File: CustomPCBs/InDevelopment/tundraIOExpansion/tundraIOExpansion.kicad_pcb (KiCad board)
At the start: 4 copper layers, 46 x 36.5 mm, 54 parts, among them J1 Conn_01x25, J2 Conn_ARM_SWD_TagConnect_TC203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, J3 Conn_ARM_SWD_TagConnect_TC203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, U1 RP2040, U2 MX25L3233FM2, U4 MX25L3233FM2, U5 RP2040, Y1 12.000MHz, Y2 12.000MHz, Y3 32.768kHz

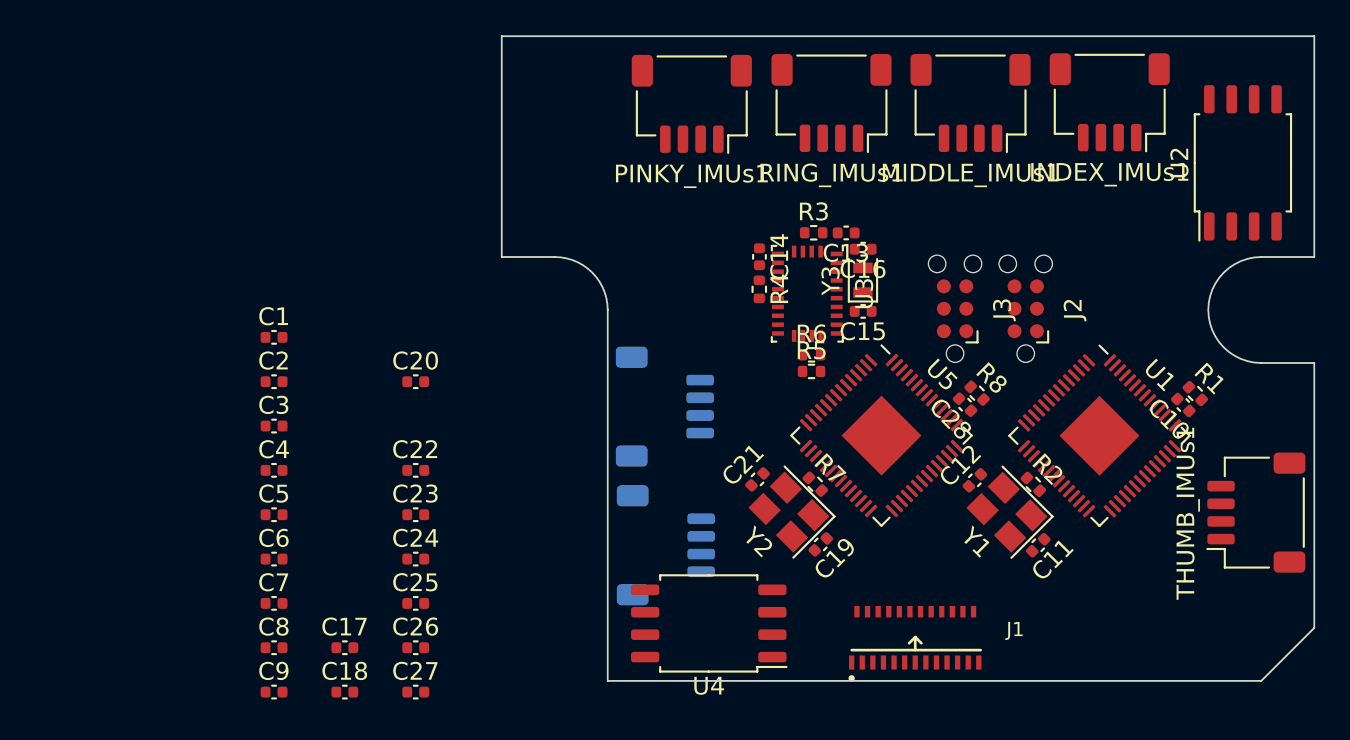
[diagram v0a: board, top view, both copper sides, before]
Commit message: Component placement complete
Will still experiment with inputs first so I know what kind of
connectors will be needed to get whatever buttons or joysticks may be
inplemented. Only after that's done will the routing of the tracks
start.
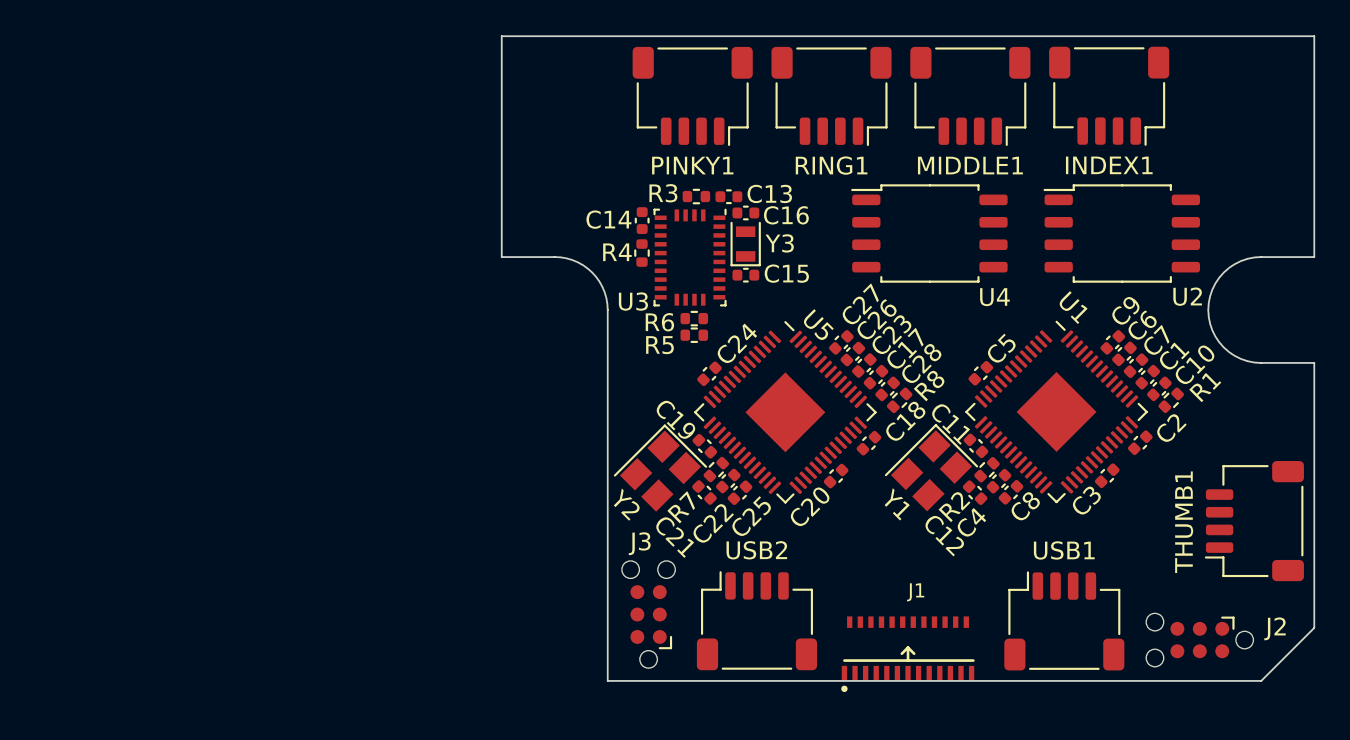
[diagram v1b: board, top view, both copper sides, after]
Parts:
- USB1, USB2: moved to F.Cu
- moved C9 51.4 mm to (150.4, 73.9), turned to 45 degrees
- moved C7 50.6 mm to (151.7, 75.2), turned to 45 degrees
- moved C6 49.5 mm to (151.0, 74.6), turned to 45 degrees
- moved C1 49.5 mm to (152.4, 75.9), turned to 45 degrees
- moved C2 49.2 mm to (151.9, 79.6), turned to -135 degrees
- moved C3 47.3 mm to (150.1, 81.5), turned to 45 degrees
- moved C8 42.6 mm to (144.6, 82.4), turned to -135 degrees
- moved C4 41.0 mm to (143.9, 81.8), turned to -135 degrees
- moved C5 40.8 mm to (142.9, 75.7), turned to -135 degrees
- moved C17 33.7 mm to (137.0, 75.9), turned to 45 degrees
- moved C18 32.8 mm to (136.6, 79.6), turned to -135 degrees
- moved C27 31.2 mm to (135.0, 73.9), turned to 45 degrees
- moved C26 29.8 mm to (135.7, 74.6), turned to 45 degrees
- moved C23 26.8 mm to (136.3, 75.2), turned to 45 degrees
- moved USB1 25.7 mm to (147.6, 89.7), turned to 0 degrees
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- renumbered INDEX_IMUs1 to INDEX1, MIDDLE_IMUs1 to MIDDLE1, PINKY_IMUs1 to PINKY1, RING_IMUs1 to RING1, THUMB_IMUs1 to THUMB1

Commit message: Adding auxiliary connectors for mixed inputs
I am still not sure what input types I will have, but I am preparing the
board to be flexible, exposing 8 GPIOs, 4 of which are analog to digital
converters.

I have also started to design the hardware interface with a second board
that can be placed below the main one, to add two rp2040 to the project
if needed.
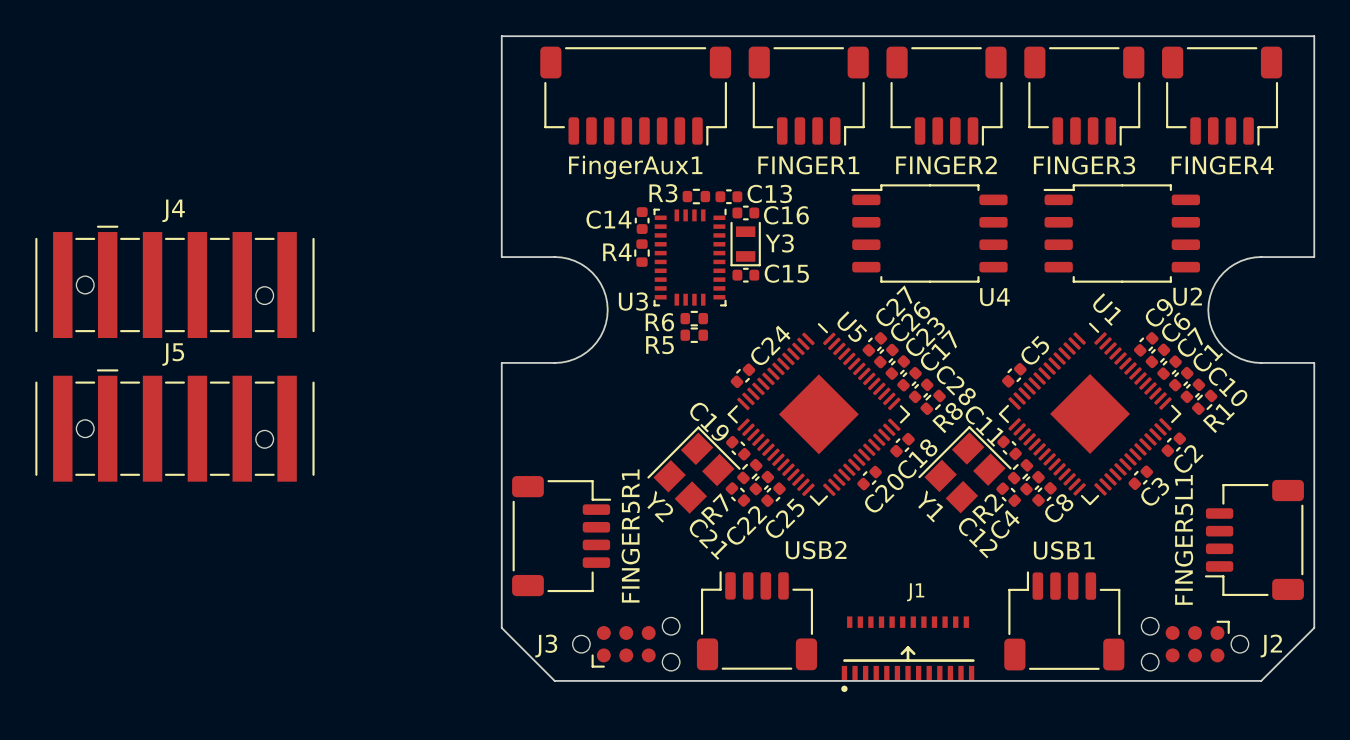
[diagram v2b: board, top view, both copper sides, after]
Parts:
- removed INDEX1, MIDDLE1, PINKY1, RING1, THUMB1: Conn_01x04, Connector_JST:JST_SH_SM04B-SRSS-TB_1x04-1MP_P1.00mm_Horizontal
- added FINGER1: Conn_01x04, Connector_JST:JST_SH_SM04B-SRSS-TB_1x04-1MP_P1.00mm_Horizontal, F.Cu at (133.2, 60.0)
- added FINGER2: Conn_01x04, Connector_JST:JST_SH_SM04B-SRSS-TB_1x04-1MP_P1.00mm_Horizontal, F.Cu at (141.0, 60.0)
- added FINGER3: Conn_01x04, Connector_JST:JST_SH_SM04B-SRSS-TB_1x04-1MP_P1.00mm_Horizontal, F.Cu at (148.8, 60.0)
- added FINGER4: Conn_01x04, Connector_JST:JST_SH_SM04B-SRSS-TB_1x04-1MP_P1.00mm_Horizontal, F.Cu at (156.6, 60.0)
- added FINGER5L1: Conn_01x04, Connector_JST:JST_SH_SM04B-SRSS-TB_1x04-1MP_P1.00mm_Horizontal, F.Cu at (158.4, 85.1)
- added FINGER5R1: Conn_01x04, Connector_JST:JST_SH_SM04B-SRSS-TB_1x04-1MP_P1.00mm_Horizontal, F.Cu at (119.1, 84.9)
- added FingerAux1: Conn_01x08, Connector_JST:JST_SH_SM08B-SRSS-TB_1x08-1MP_P1.00mm_Horizontal, F.Cu at (123.4, 60.0)
- added J4: 2211SM-04G-B1-TB, Connector_Harting:Harting_har-flexicon_14110413001xxx_1x04-MP_P2.54mm_Vertical, F.Cu at (97.3, 70.7)
- added J5: 2211SM-04G-B1-TB, Connector_Harting:Harting_har-flexicon_14110413001xxx_1x04-MP_P2.54mm_Vertical, F.Cu at (97.3, 78.8)
- moved J3 2.10 mm to (122.8, 91.0), turned to 0 degrees
- moved C10 1.90 mm to (154.9, 76.7)
- moved C12 1.90 mm to (144.5, 82.5)
- moved C18 1.90 mm to (138.5, 79.7)
- moved C23 1.90 mm to (138.2, 75.3)
- moved C6 1.90 mm to (152.9, 74.7)
- moved R7 1.90 mm to (129.8, 81.2)
- moved R8 1.90 mm to (140.2, 77.3)
- moved U5 1.90 mm to (133.7, 78.0)
- moved Y1 1.90 mm to (142.0, 81.3)
- moved C8 1.90 mm to (146.5, 82.5)
- moved C19 1.90 mm to (129.2, 79.9)
- moved C24 1.90 mm to (129.4, 75.8)
- moved Y2 1.90 mm to (126.7, 81.3)
- moved C1 1.90 mm to (154.2, 76.0)
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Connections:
- U1 pad 27: unconnected-(U1-GPIO16-Pad27) -> INTER_RP2040_UART_TX2
- U1 pad 28: unconnected-(U1-GPIO17-Pad28) -> INTER_RP2040_UART_RX2
- U1 pad 6: unconnected-(U1-GPIO4-Pad6) -> INTER_RP2040_UART_TX1
- U1 pad 7: unconnected-(U1-GPIO5-Pad7) -> INTER_RP2040_UART_RX1
- U5 pad 16: unconnected-(U5-GPIO13-Pad16) -> INTER_RP2040_UART_TX3
- U5 pad 17: unconnected-(U5-GPIO14-Pad17) -> INTER_RP2040_UART_RX3
- U5 pad 34: unconnected-(U5-GPIO22-Pad34) -> Net-(FingerAux1-Pin_1)
- U5 pad 35: unconnected-(U5-GPIO23-Pad35) -> Net-(FingerAux1-Pin_2)
- U5 pad 36: unconnected-(U5-GPIO24-Pad36) -> Net-(FingerAux1-Pin_3)
- U5 pad 37: unconnected-(U5-GPIO25-Pad37) -> Net-(FingerAux1-Pin_4)
- U5 pad 38: unconnected-(U5-GPIO26_ADC0-Pad38) -> Net-(FingerAux1-Pin_5)
- U5 pad 39: unconnected-(U5-GPIO27_ADC1-Pad39) -> Net-(FingerAux1-Pin_6)
- U5 pad 40: unconnected-(U5-GPIO28_ADC2-Pad40) -> Net-(FingerAux1-Pin_7)
- U5 pad 41: unconnected-(U5-GPIO29_ADC3-Pad41) -> Net-(FingerAux1-Pin_8)
- U5 pad 6: unconnected-(U5-GPIO4-Pad6) -> INTER_RP2040_UART_TX1
- U5 pad 7: unconnected-(U5-GPIO5-Pad7) -> INTER_RP2040_UART_RX1
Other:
- outline, holes or cut-outs redrawn

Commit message: Updating components' 3d models for 3d print cases
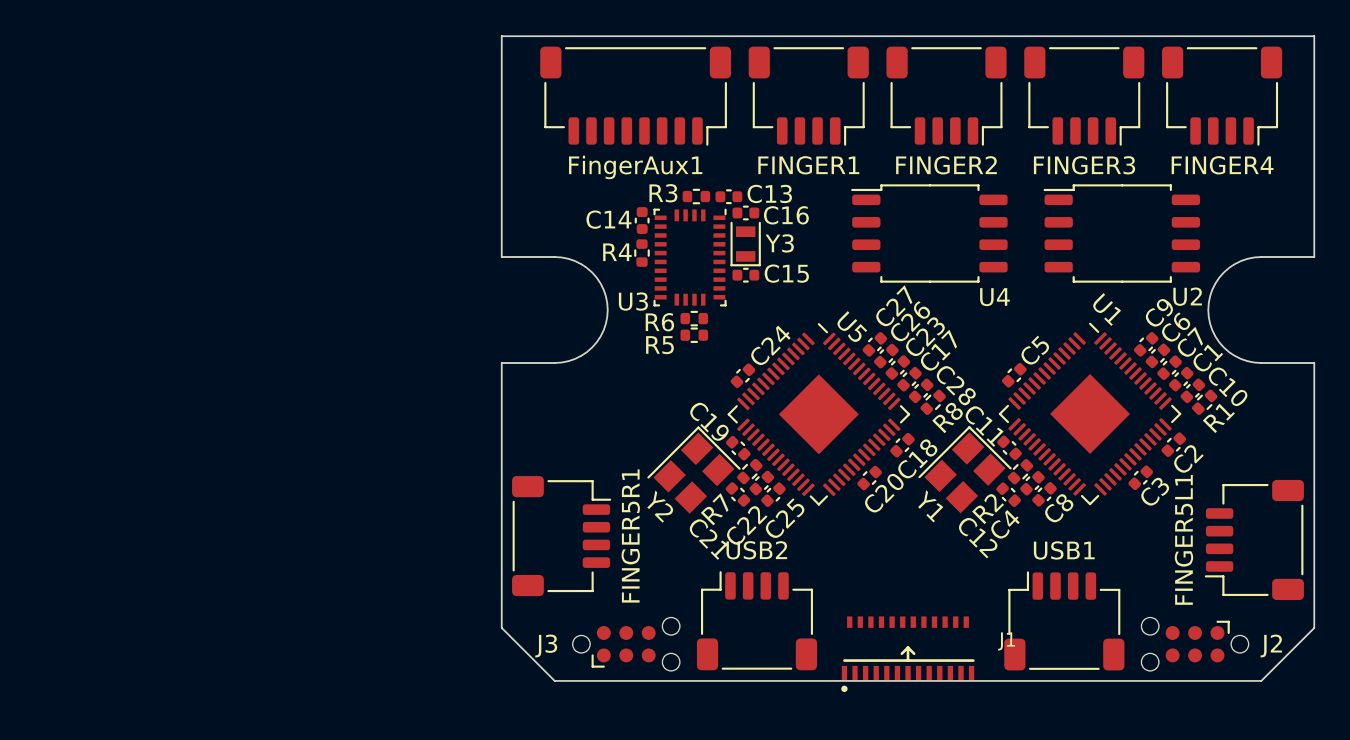
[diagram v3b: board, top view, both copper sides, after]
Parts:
- removed J4, J5: 2211SM-04G-B1-TB, Connector_Harting:Harting_har-flexicon_14110413001xxx_1x04-MP_P2.54mm_Vertical
- FINGER1, FINGER2, FINGER3, FINGER4, FINGER5L1, FINGER5R1, USB1, USB2: footprint Connector_JST:JST_SH_SM04B-SRSS-TB_1x04-1MP_P1.00mm_Horizontal -> my_connectors:JST_SH_SM04B-SRSS-TB_1x04-1MP_P1.00mm_Horizontal
- FingerAux1: footprint Connector_JST:JST_SH_SM08B-SRSS-TB_1x08-1MP_P1.00mm_Horizontal -> my_connectors:JST_SH_SM08B-SRSS-TB_1x08-1MP_P1.00mm_Horizontal
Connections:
- U1 pad 27: INTER_RP2040_UART_TX2 -> unconnected-(U1-GPIO16-Pad27)
- U1 pad 28: INTER_RP2040_UART_RX2 -> unconnected-(U1-GPIO17-Pad28)
- U5 pad 16: INTER_RP2040_UART_TX3 -> unconnected-(U5-GPIO13-Pad16)
- U5 pad 17: INTER_RP2040_UART_RX3 -> unconnected-(U5-GPIO14-Pad17)
- U5 pad 6: INTER_RP2040_UART_TX1 -> INTER_RP2040_UART_RX1
- U5 pad 7: INTER_RP2040_UART_RX1 -> INTER_RP2040_UART_TX1

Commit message: Saving work on the interface board
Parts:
- moved C25 2.66 mm to (128.8, 83.7)
- moved C8 2.60 mm to (144.2, 83.7)
- moved C21 1.16 mm to (128.1, 83.0), turned to -135 degrees
- moved C12 1.08 mm to (143.5, 83.0), turned to -135 degrees
- moved C9 1.00 mm to (153.0, 73.3)
- moved C27 0.96 mm to (137.6, 73.4)
- moved C22 0.70 mm to (130.1, 82.4)
- moved R7 0.65 mm to (129.4, 81.8)
- moved C19 0.65 mm to (128.8, 80.4)
- moved Y2 0.65 mm to (126.3, 81.8)
- moved R2 0.56 mm to (144.8, 81.7)
- moved Y1 0.56 mm to (141.7, 81.8)
- moved C11 0.56 mm to (144.2, 80.3)
- moved C4 0.56 mm to (145.5, 82.3)
- moved U2 0.34 mm to (150.6, 67.8)
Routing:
- net GND: track 0.00 -> 62.0 mm, vias 0 -> 27
- net +3V3: track 0.00 -> 38.5 mm, vias 0 -> 20
- net D11-MI_MOSI: track 0.00 -> 22.7 mm, vias 0 -> 2
- net D10-MI_CS: track 0.00 -> 21.7 mm
- net +1V1: track 0.00 -> 20.6 mm
- net Net-(J3-~{RESET}): track 0.00 -> 17.4 mm, vias 0 -> 2
- net D12-MI_MISO: track 0.00 -> 17.1 mm, vias 0 -> 2
- net D13-MI_SCLK: track 0.00 -> 16.6 mm
- net Net-(J3-SWDIO): track 0.00 -> 15.9 mm
- net Net-(U4-~{HOLD}/SIO3): track 0.00 -> 15.9 mm
- net Net-(J2-SWDIO): track 0.00 -> 15.8 mm, vias 0 -> 2
- net Net-(J3-SWCLK): track 0.00 -> 15.6 mm, vias 0 -> 2
- net Net-(J2-SWCLK): track 0.00 -> 15.5 mm, vias 0 -> 2
- net Net-(U4-SCLK): track 0.00 -> 13.7 mm
- net Net-(J2-~{RESET}): track 0.00 -> 12.7 mm, vias 0 -> 2
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- added copper zone on In1.Cu, net +3V3
- added copper zone on In2.Cu, net GND

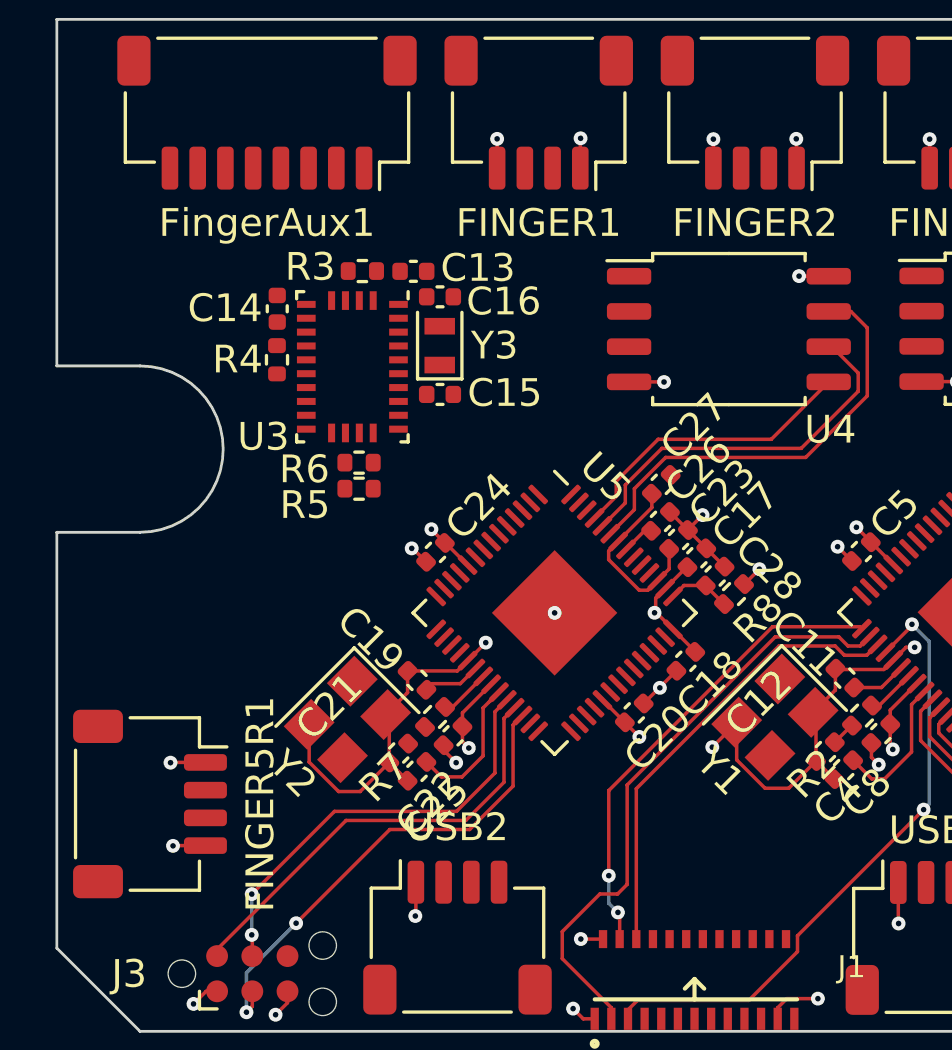
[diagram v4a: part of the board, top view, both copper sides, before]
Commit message: More rounting done on the expansion card
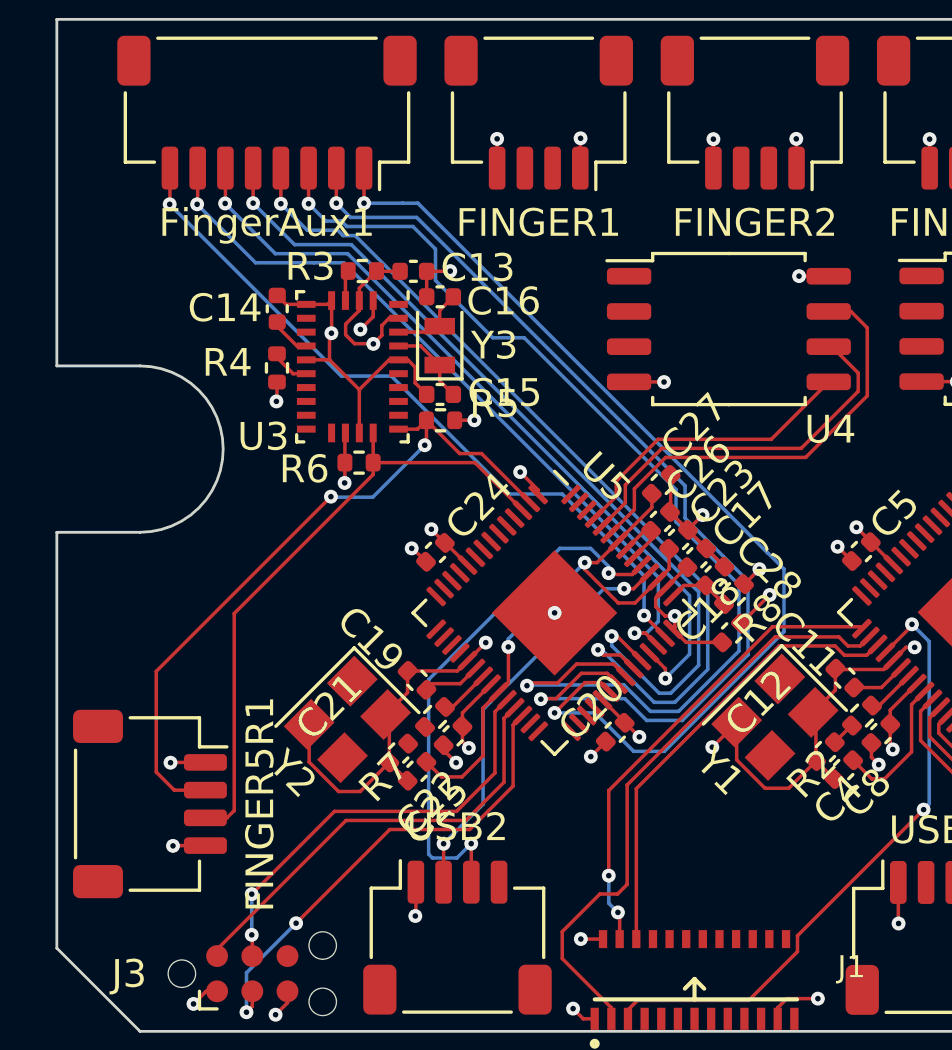
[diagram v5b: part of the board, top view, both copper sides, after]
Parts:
- moved R5 3.84 mm to (129.6, 71.0), turned to 180 degrees
- moved C18 1.94 mm to (140.1, 78.7), turned to 45 degrees
- moved C20 0.98 mm to (135.9, 82.3), turned to -135 degrees
- moved R4 0.29 mm to (123.7, 69.2), turned to 90 degrees
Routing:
- net Net-(FingerAux1-Pin_3): track 0.00 -> 39.3 mm, vias 0 -> 2
- net Net-(FingerAux1-Pin_1): track 0.00 -> 37.4 mm, vias 0 -> 2
- net Net-(FingerAux1-Pin_2): track 0.00 -> 37.2 mm, vias 0 -> 2
- net Net-(FingerAux1-Pin_4): track 0.00 -> 32.5 mm, vias 0 -> 2
- net Net-(FingerAux1-Pin_5): track 0.00 -> 31.8 mm, vias 0 -> 2
- net Net-(FingerAux1-Pin_6): track 0.00 -> 28.4 mm, vias 0 -> 2
- net Net-(FingerAux1-Pin_7): track 0.00 -> 27.1 mm, vias 0 -> 2
- net Net-(FingerAux1-Pin_8): track 0.00 -> 26.5 mm, vias 0 -> 2
- net Net-(FINGER5L1-Pin_2): track 0.00 -> 25.8 mm, vias 0 -> 2
- net Net-(FINGER5L1-Pin_3): track 0.00 -> 22.9 mm
- net Net-(U5-USB_DP): track 0.00 -> 19.8 mm, vias 0 -> 2
- net GND: track 62.0 -> 78.8 mm, vias 27 -> 31
- net Net-(U5-USB_DM): track 0.00 -> 14.9 mm, vias 0 -> 2
- net +3V3: track 38.5 -> 51.5 mm, vias 20 -> 25
- net +1V1: track 20.6 -> 28.6 mm, vias 0 -> 2
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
